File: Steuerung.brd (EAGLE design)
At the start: 114.3 x 53.3 mm, 3 parts

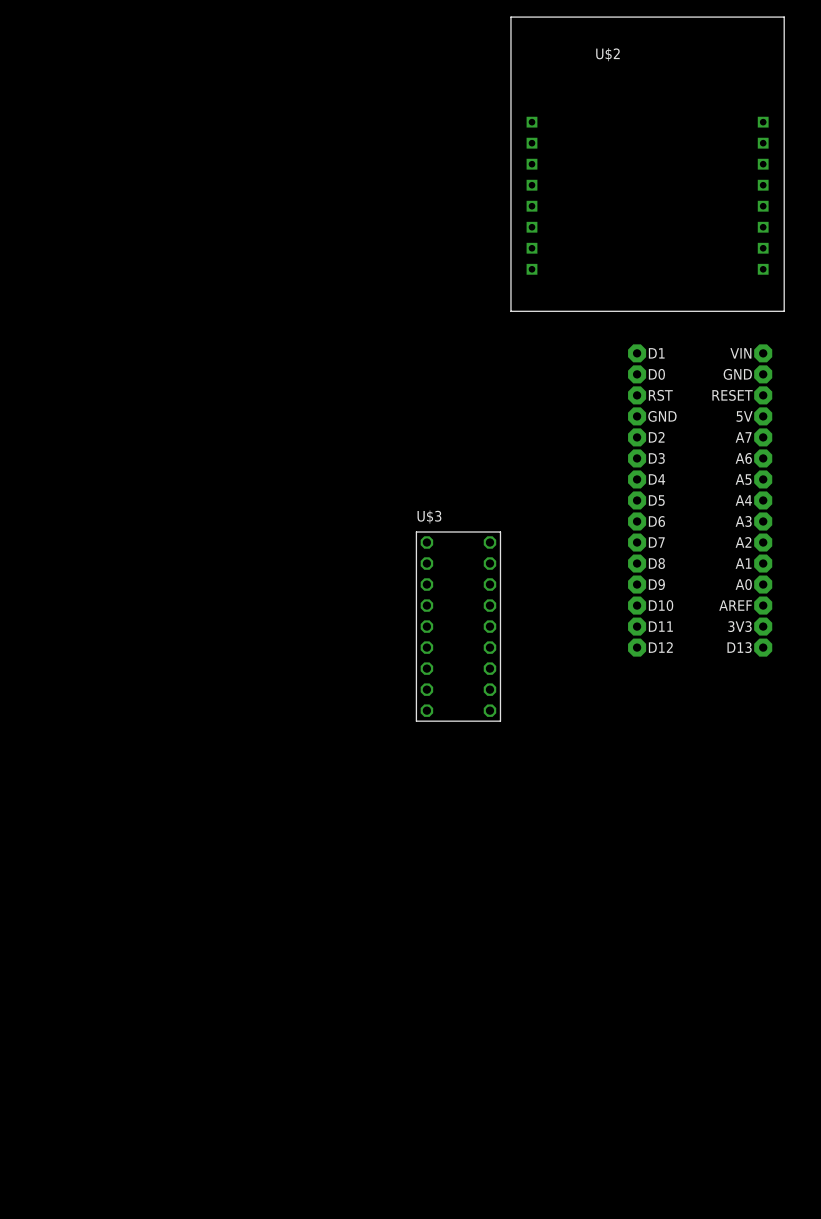
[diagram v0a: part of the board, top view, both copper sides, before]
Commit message: Schaltplan für 16MHz/5V Nano und ESP-Witty adaptiert
Signed-off-by: Wolfgang Kraft <fablab-ka@wkraft.org>
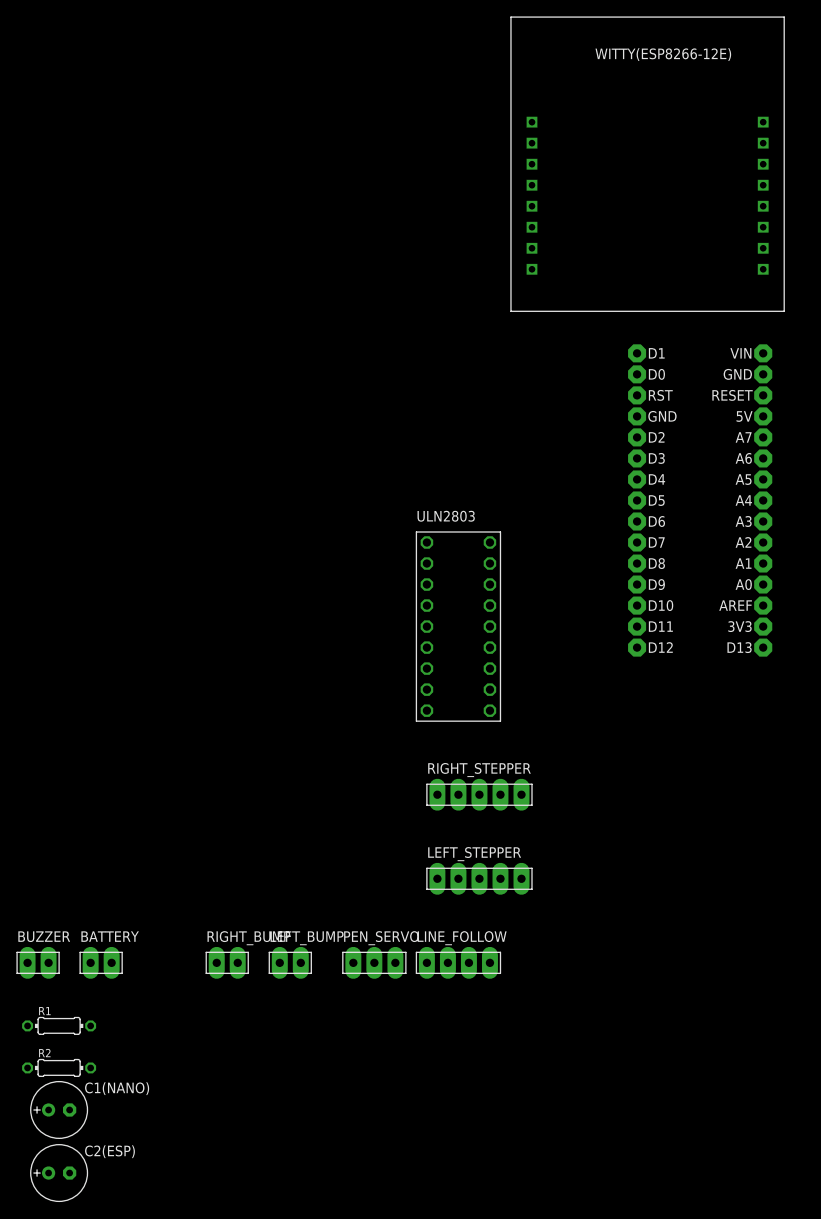
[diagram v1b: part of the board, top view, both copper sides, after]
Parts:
- added BATTERY, BUZZER, LEFT_BUMP, RIGHT_BUMP: CON_22.54, pcaroli:CON_2_2.54
- added C1(NANO), C2(ESP): 470µ, resistor:E2,5-7
- added LEFT_STEPPER, RIGHT_STEPPER: CON_5, pcaroli:CON_5_2.54
- added LINE_FOLLOW: CON_4, pcaroli:CON_4_2.54
- added PEN_SERVO: CON_3, pcaroli:CON_3_2.54
- added R1: 100, resistor:0204/7
- added R2: 200, resistor:0204/7
- renumbered U$1 to ARDUINO_NANO, U$2 to WITTY(ESP8266-12E), U$3 to ULN2803
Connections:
- new net GND: ARDUINO_NANO.GND, ARDUINO_NANO.GND2, BATTERY.P$2, BUZZER.P$2, C1(NANO).-, C2(ESP).-, LEFT_BUMP.P$1, LINE_FOLLOW.P$1, PEN_SERVO.P$3, R2.2, RIGHT_BUMP.P$1, ULN2803.P$9, WITTY(ESP8266-12E).P$9
- new net N$1: LEFT_STEPPER.P$1, ULN2803.P$18
- new net N$10: ARDUINO_NANO.D10, ULN2803.P$2
- new net N$11: ARDUINO_NANO.D11, ULN2803.P$3
- new net N$12: ARDUINO_NANO.D12, ULN2803.P$4
- new net N$13: ARDUINO_NANO.D4, ULN2803.P$5
- new net N$14: ARDUINO_NANO.D5, ULN2803.P$6
- new net N$15: ARDUINO_NANO.D6, ULN2803.P$7
- new net N$16: ARDUINO_NANO.D7, ULN2803.P$8
- new net N$17: ARDUINO_NANO.A3, LEFT_BUMP.P$2
- new net N$18: ARDUINO_NANO.A2, RIGHT_BUMP.P$2
- new net N$19: ARDUINO_NANO.D0, R1.2
- new net N$2: LEFT_STEPPER.P$2, ULN2803.P$17
- new net N$20: R1.1, R2.1, WITTY(ESP8266-12E).P$15
- new net N$21: ARDUINO_NANO.D1, WITTY(ESP8266-12E).P$16
- new net N$22: ARDUINO_NANO.RESET, ARDUINO_NANO.RST, WITTY(ESP8266-12E).P$14
- new net N$23: ARDUINO_NANO.D9, BUZZER.P$1
- new net N$24: ARDUINO_NANO.D3, PEN_SERVO.P$1
- new net N$25: ARDUINO_NANO.A1, LINE_FOLLOW.P$4
- new net N$26: ARDUINO_NANO.A0, LINE_FOLLOW.P$3
- new net N$27: ARDUINO_NANO.+5V, LINE_FOLLOW.P$2
- new net N$3: LEFT_STEPPER.P$3, ULN2803.P$16
- new net N$4: LEFT_STEPPER.P$4, ULN2803.P$15
- new net N$5: RIGHT_STEPPER.P$1, ULN2803.P$14
- new net N$6: RIGHT_STEPPER.P$2, ULN2803.P$13
- new net N$7: RIGHT_STEPPER.P$3, ULN2803.P$12
- new net N$8: RIGHT_STEPPER.P$4, ULN2803.P$11
- new net N$9: ARDUINO_NANO.D8, ULN2803.P$1
- new net VSS: ARDUINO_NANO.VIN, BATTERY.P$1, C1(NANO).+, C2(ESP).+, PEN_SERVO.P$2, ULN2803.P$10, WITTY(ESP8266-12E).P$8

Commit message: minor correction
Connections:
- net VSS: now also LEFT_STEPPER.P$5, RIGHT_STEPPER.P$5
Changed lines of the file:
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@@
 <contactref element="C1(NANO)" pad="+"/>
 <contactref element="C2(ESP)" pad="+"/>
+<contactref element="RIGHT_STEPPER" pad="P$5"/>
+<contactref element="LEFT_STEPPER" pad="P$5"/>
 <wire x1="-102.87" y1="-50.8" x2="-102.87" y2="-58.42" width="0" layer="19" extent="1-1"/>
 <wire x1="-97.79" y1="-33.02" x2="-102.87" y2="-50.8" width="0" layer="19" extent="1-1"/>
 <wire x1="-63.5" y1="-33.02" x2="-97.79" y2="-33.02" width="0" layer="19" extent="1-1"/>
-<wire x1="-49.53" y1="-2.54" x2="-63.5" y2="-33.02" width="0" layer="19" extent="1-1"/>
+<wire x1="-45.72" y1="-22.86" x2="-63.5" y2="-33.02" width="0" layer="19" extent="1-1"/>
+<wire x1="-45.72" y1="-12.7" x2="-45.72" y2="-22.86" width="0" layer="19" extent="1-1"/>
+<wire x1="-49.53" y1="-2.54" x2="-45.72" y2="-12.7" width="0" layer="19" extent="1-1"/>
 <wire x1="-44.45" y1="50.8" x2="-49.53" y2="-2.54" width="0" layer="19" extent="1-1"/>
 <wire x1="-16.51" y1="40.64" x2="-44.45" y2="50.8" width="0" layer="19" extent="1-1"/>

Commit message: First PCB
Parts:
- moved C2(ESP) 207.3 mm to (90.2, 20.3), turned to 180 degrees
- moved RIGHT_BUMP 189.3 mm to (100.3, 20.3), turned to 180 degrees
- moved C1(NANO) 156.3 mm to (20.3, 47.0), turned to 270 degrees
- moved PEN_SERVO 147.2 mm to (73.7, 20.3)
- moved R1 147.1 mm to (30.5, 24.1), turned to 90 degrees
- moved R2 142.0 mm to (24.1, 20.3), turned to 180 degrees
- moved LEFT_STEPPER 139.5 mm to (86.4, 2.54)
- moved BUZZER 128.2 mm to (2.54, 38.1), turned to 180 degrees
- moved BATTERY 126.5 mm to (2.54, 45.7), turned to 180 degrees
- moved WITTY(ESP8266-12E) 119.1 mm to (72.4, 45.7)
- moved LINE_FOLLOW 110.0 mm to (50.8, 2.54)
- moved ULN2803 104.8 mm to (50.8, 19.1), turned to 270 degrees
- moved LEFT_BUMP 101.5 mm to (12.7, 20.3), turned to 180 degrees
- moved ARDUINO_NANO 72.1 mm to (45.7, 40.6), turned to 90 degrees
- moved RIGHT_STEPPER 70.3 mm to (17.8, 2.54)
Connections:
- net N$1: now also LEFT_STEPPER.P$4; no longer LEFT_STEPPER.P$1
- net N$10: now also ULN2803.P$3; no longer ULN2803.P$2
- net N$11: now also ULN2803.P$2; no longer ULN2803.P$3
- net N$12: now also ULN2803.P$1; no longer ULN2803.P$4
- net N$13: now also ARDUINO_NANO.D7; no longer ARDUINO_NANO.D4
- net N$14: now also ARDUINO_NANO.D6; no longer ARDUINO_NANO.D5
- net N$15: now also ARDUINO_NANO.D5; no longer ARDUINO_NANO.D6
- net N$16: now also ARDUINO_NANO.D4; no longer ARDUINO_NANO.D7
- net N$2: now also LEFT_STEPPER.P$3; no longer LEFT_STEPPER.P$2
- net N$3: now also LEFT_STEPPER.P$2; no longer LEFT_STEPPER.P$3
- net N$4: now also LEFT_STEPPER.P$1; no longer LEFT_STEPPER.P$4
- net N$5: now also RIGHT_STEPPER.P$4; no longer RIGHT_STEPPER.P$1
- net N$6: now also RIGHT_STEPPER.P$3; no longer RIGHT_STEPPER.P$2
- net N$7: now also RIGHT_STEPPER.P$2; no longer RIGHT_STEPPER.P$3
- net N$8: now also RIGHT_STEPPER.P$1; no longer RIGHT_STEPPER.P$4
- net N$9: now also ULN2803.P$4; no longer ULN2803.P$1
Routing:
- net GND: track 0.00 -> 252.4 mm, vias 0 -> 6
- net VSS: track 0.00 -> 242.6 mm
- net N$18: track 0.00 -> 116.8 mm
- net N$20: track 0.00 -> 113.0 mm
- net N$21: track 0.00 -> 87.8 mm, vias 0 -> 2
- net N$27: track 0.00 -> 87.6 mm, vias 0 -> 2
- net N$22: track 0.00 -> 80.5 mm, vias 0 -> 2
- net N$26: track 0.00 -> 74.9 mm, vias 0 -> 2
- net N$17: track 0.00 -> 74.9 mm, vias 0 -> 2
- net N$25: track 0.00 -> 69.9 mm, vias 0 -> 2
- net N$23: track 0.00 -> 57.1 mm
- net N$8: track 0.00 -> 43.2 mm
- net N$7: track 0.00 -> 41.7 mm
- net N$24: track 0.00 -> 40.4 mm, vias 0 -> 2
- net N$6: track 0.00 -> 40.2 mm
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- added copper zone on layer 16, net GND--
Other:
- outline, holes or cut-outs redrawn

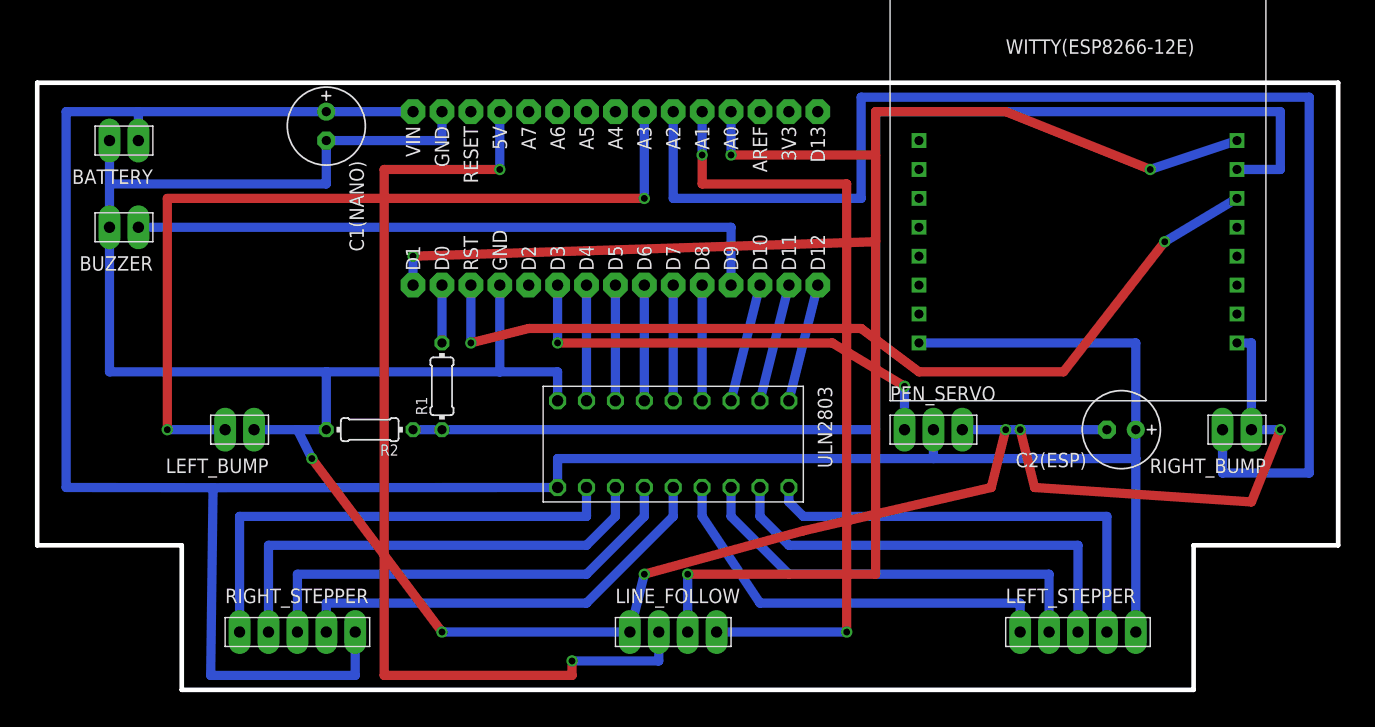
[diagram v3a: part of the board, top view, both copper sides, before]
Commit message: optimized Layout
Bigger Vias and Pads, stylish 45°-edges ;)
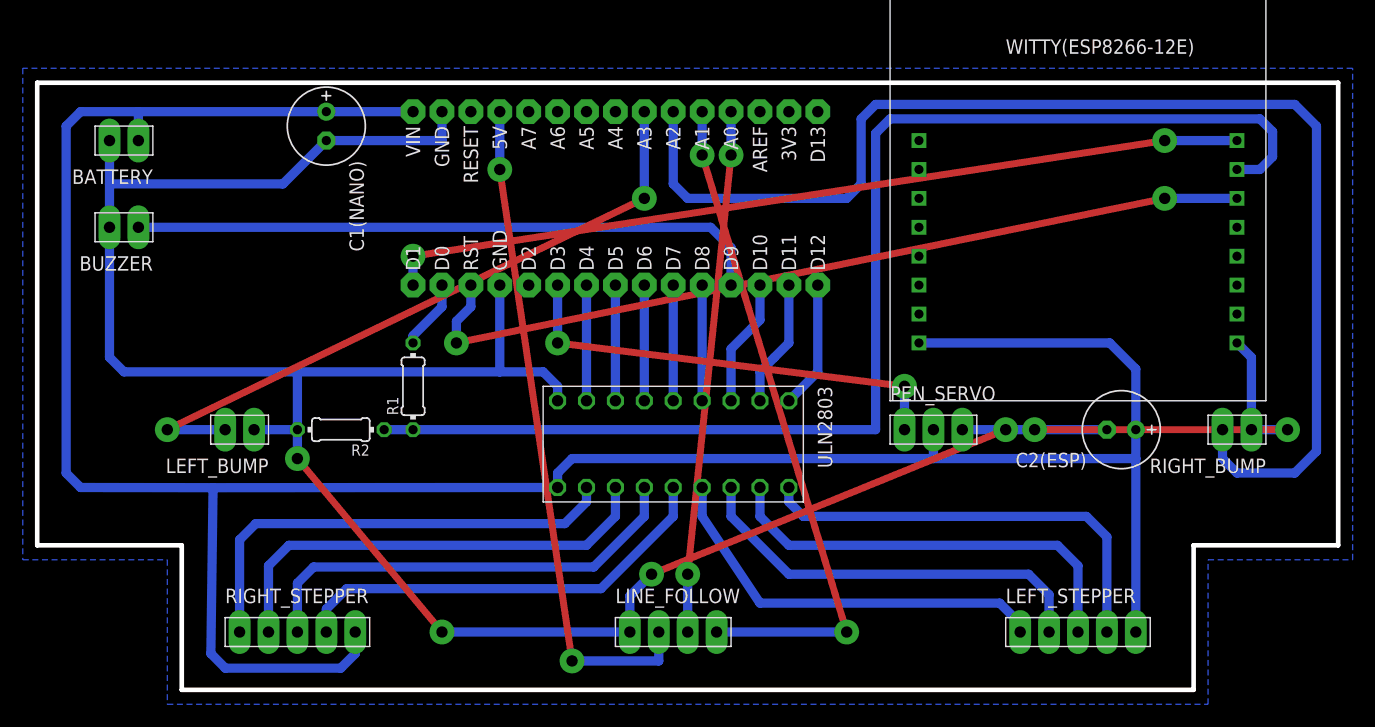
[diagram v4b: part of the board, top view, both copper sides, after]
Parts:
- moved R1 2.54 mm to (27.9, 24.1)
- moved R2 2.54 mm to (21.6, 20.3)
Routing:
- net N$26: track 74.9 -> 45.9 mm
- net N$27: track 87.6 -> 58.9 mm
- net GND: track 252.4 -> 235.2 mm
- net N$17: track 74.9 -> 59.3 mm
- net N$21: track 87.8 -> 75.7 mm
- net N$25: track 69.9 -> 59.0 mm
- net VSS: track 242.6 -> 236.2 mm
- net N$18: track 116.8 -> 111.6 mm
- net N$22: track 80.5 -> 75.5 mm
- net N$20: track 113.0 -> 110.9 mm
- net N$8: track 43.2 -> 41.2 mm
- net N$19: track 5.08 -> 6.13 mm
- net N$1: track 39.9 -> 38.8 mm
- net N$4: track 37.1 -> 36.0 mm
- net N$3: track 37.7 -> 36.6 mm
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- added copper zone on layer 16, net GND
- removed copper zone on layer 16, net GND--

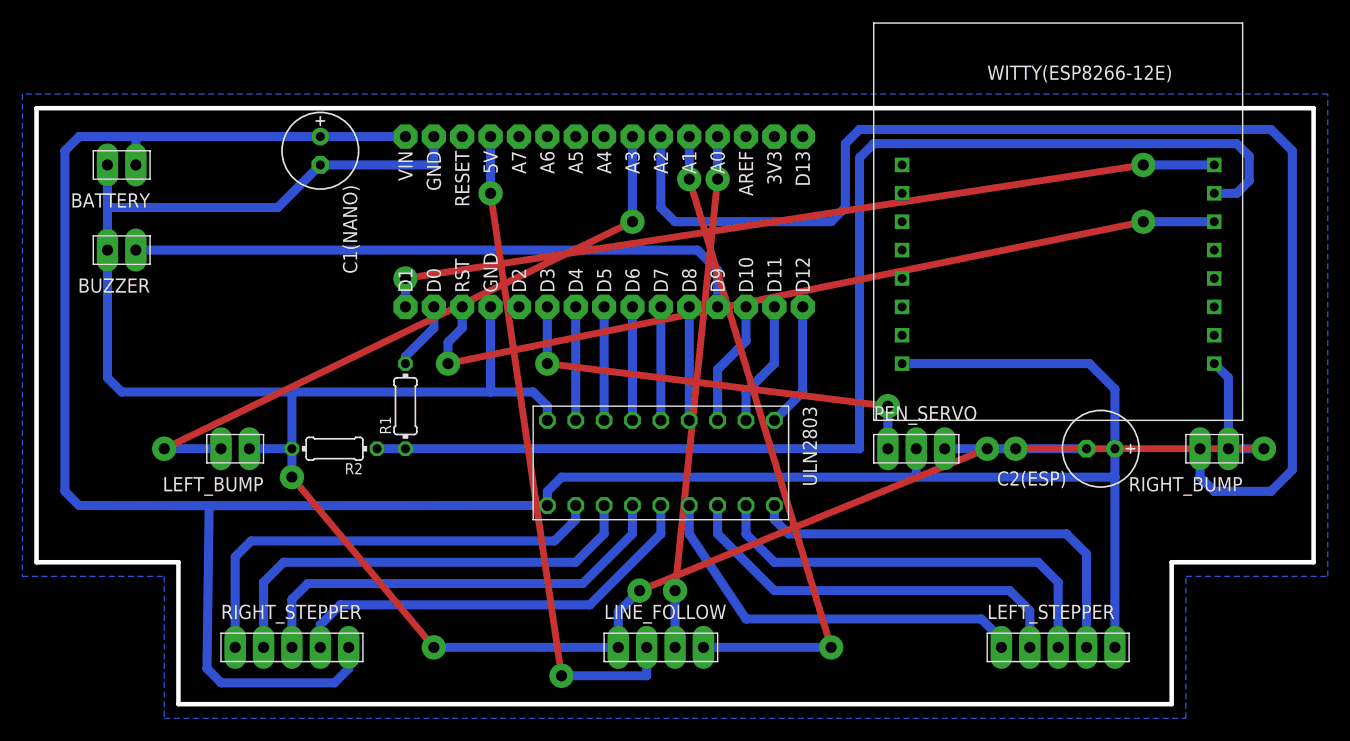
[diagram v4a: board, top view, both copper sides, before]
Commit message: PCB resize, origin point fix
PCB compressed (Y-axis) to fit 2 PCBs on a 160x100cm Sheet.
Adjusted origin point in Y-Axis.
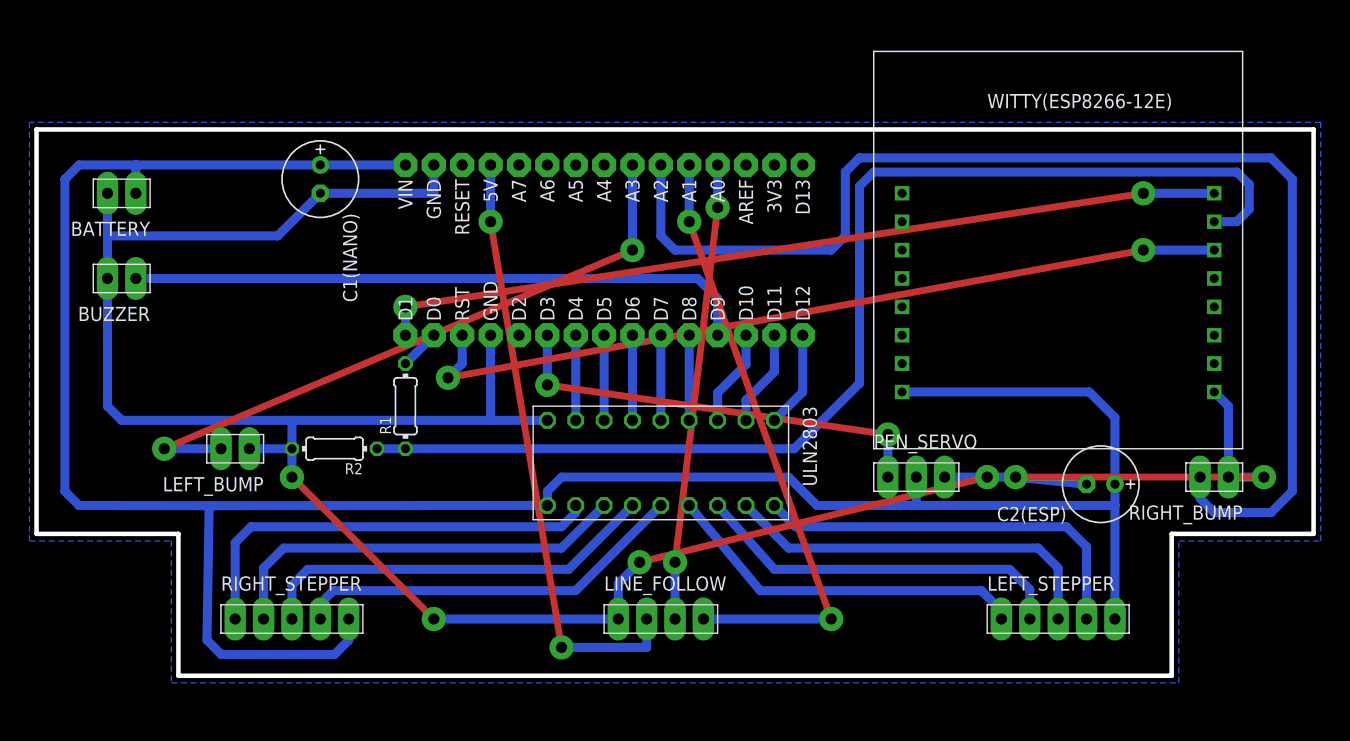
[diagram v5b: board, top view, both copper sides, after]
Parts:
- moved C2(ESP) 3.18 mm to (90.2, 17.1)
- moved LEFT_STEPPER 2.54 mm to (86.4, 5.08)
- moved LINE_FOLLOW 2.54 mm to (50.8, 5.08)
- moved RIGHT_STEPPER 2.54 mm to (17.8, 5.08)
- moved ARDUINO_NANO 2.54 mm to (45.7, 38.1)
- moved BATTERY 2.54 mm to (2.54, 43.2)
- moved BUZZER 2.54 mm to (2.54, 35.6)
- moved C1(NANO) 2.54 mm to (20.3, 44.5)
- moved PEN_SERVO 2.54 mm to (73.7, 17.8)
- moved RIGHT_BUMP 2.54 mm to (100.3, 17.8)
- moved WITTY(ESP8266-12E) 2.54 mm to (72.4, 43.2)
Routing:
- net VSS: track 236.2 -> 227.1 mm
- net GND: track 235.2 -> 227.4 mm
- net N$20: track 110.9 -> 104.9 mm
- net N$26: track 45.9 -> 40.9 mm
- net N$27: track 58.9 -> 53.9 mm
- net N$25: track 59.0 -> 54.3 mm
- net N$7: track 40.6 -> 37.4 mm
- net N$6: track 39.7 -> 36.5 mm
- net N$2: track 38.1 -> 34.8 mm
- net N$4: track 36.0 -> 33.0 mm
- net N$5: track 38.4 -> 35.5 mm
- net N$1: track 38.8 -> 35.9 mm
- net N$3: track 36.6 -> 33.9 mm
- net N$9: track 10.2 -> 7.62 mm
- net N$16: track 10.2 -> 7.62 mm
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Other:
- board size 114.3 x 53.3 mm -> 114.3 x 48.9 mm
